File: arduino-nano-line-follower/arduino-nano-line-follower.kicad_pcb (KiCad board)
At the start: 2 copper layers, 0 parts

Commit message: project 9 / arduino nano line follower / added pcb
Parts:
- added 9V L298N: 9v_gnd_l293d, Connector_PinSocket_2.54mm:PinSocket_1x02_P2.54mm_Vertical, F.Cu at (112.8, 81.3)
- added A1: Arduino_Nano_Every, Module:Arduino_Nano, F.Cu at (93.5, 46.0)
- added ARD PWR: arduino_vcc_gnd, Connector_PinSocket_2.54mm:PinSocket_1x02_P2.54mm_Vertical, F.Cu at (112.8, 46.5)
- added BT1: Battery, Connector_PinSocket_2.54mm:PinSocket_1x02_P2.54mm_Vertical, F.Cu at (119.3, 81.2)
- added C1: 100n, Capacitor_THT:C_Disc_D3.0mm_W1.6mm_P2.50mm, F.Cu at (112.1, 60.2)
- added C2: 10u, Capacitor_THT:C_Radial_D4.0mm_H5.0mm_P1.50mm, F.Cu at (118.2, 75.9)
- added G***: LOGO, graphics:pcb_logo_3mmx3mm, F.Cu at (103.8, 38.8)
- added G***: LOGO, graphics:pcb_logo_45mmx45mm, B.Cu at (103.8, 64.4)
- added INP L298N: l298_input_pins, Connector_PinHeader_2.54mm:PinHeader_1x04_P2.54mm_Vertical, F.Cu at (89.6, 61.3)
- added IR PWR: 5v_ir_sensors_pins, Connector_PinHeader_2.54mm:PinHeader_1x02_P2.54mm_Vertical, F.Cu at (112.9, 56.6)
- added IR SIG: ir_signal, Connector_PinHeader_2.54mm:PinHeader_1x02_P2.54mm_Vertical, F.Cu at (112.8, 64.1)
- added PWR GND: gnd_ir_sensors_pins, Connector_PinHeader_2.54mm:PinHeader_1x02_P2.54mm_Vertical, F.Cu at (112.8, 51.6)
- added PWR SW: pwr_switch, Button_Switch_THT:SW_NKK_G1xJP, F.Cu at (115.0, 76.6)
- added REF**: MountingHole_3.2mm_M3, MountingHole:MountingHole_3.2mm_M3, F.Cu at (88.2, 91.4)
- added REF**: MountingHole_3.2mm_M3, MountingHole:MountingHole_3.2mm_M3, F.Cu at (120.4, 91.5)
- added REF**: MountingHole_3.2mm_M3, MountingHole:MountingHole_3.2mm_M3, F.Cu at (120.3, 38.4)
- added REF**: MountingHole_3.2mm_M3, MountingHole:MountingHole_3.2mm_M3, F.Cu at (88.3, 38.4)
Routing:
- net Net-(A1-+5V): track 0.00 -> 11.9 mm
- net Net-(A1-A0): track 0.00 -> 9.98 mm
- net +9V: track 0.00 -> 9.35 mm
- net Net-(A1-A1): track 0.00 -> 9.02 mm
- net Net-(J5-Pin_1): track 0.00 -> 4.80 mm
- net +5V: track 0.00 -> 4.34 mm
- net Net-(A1-D7): track 0.00 -> 3.88 mm
- net Net-(A1-D5): track 0.00 -> 3.88 mm
- net Net-(A1-D4): track 0.00 -> 3.88 mm
- net Net-(A1-D6): track 0.00 -> 3.88 mm
- added copper zone on B.Cu, net GND
- added copper zone on F.Cu, net GND
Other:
- board outline added: 39.5 x 60.2 mm
- board text added: "|ARDUINO NANO LINE FOLLOWER|"

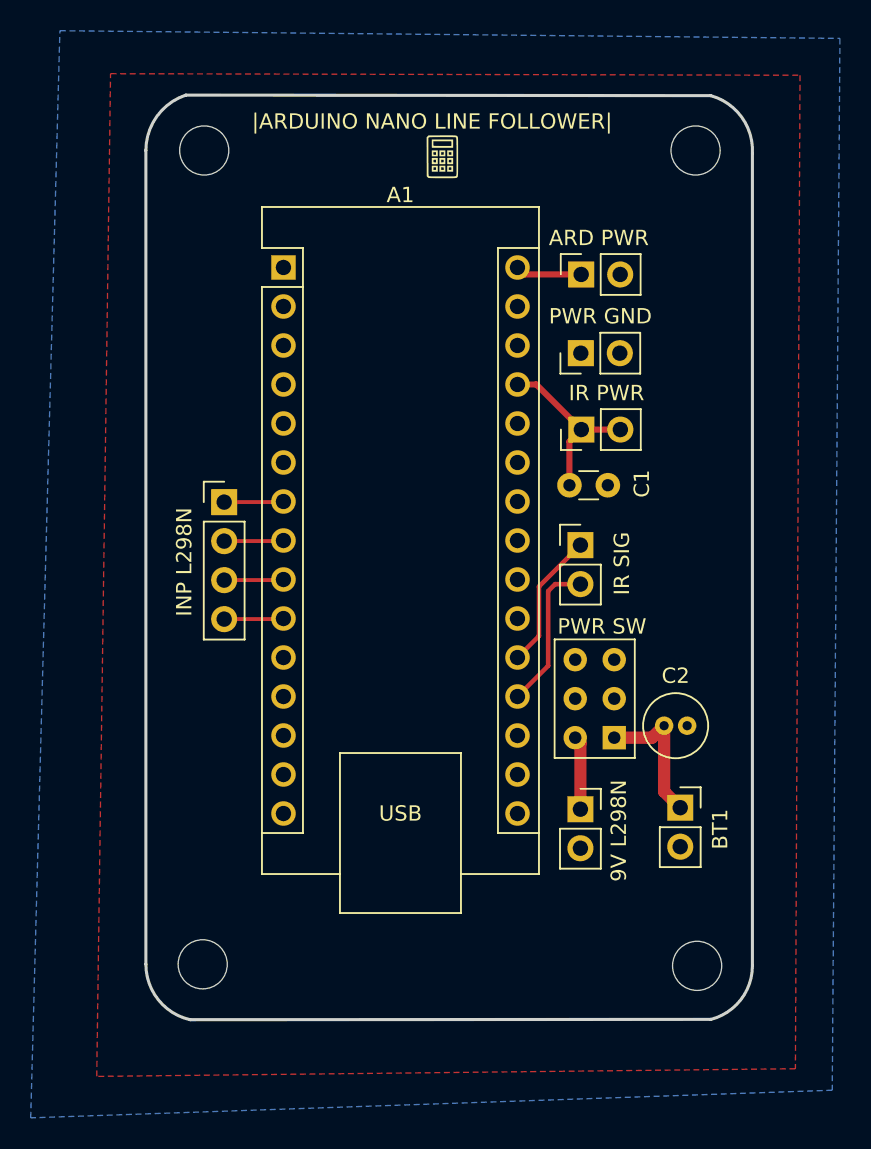
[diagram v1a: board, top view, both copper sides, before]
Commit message: project 9 / arduino nano line follower / improved connections
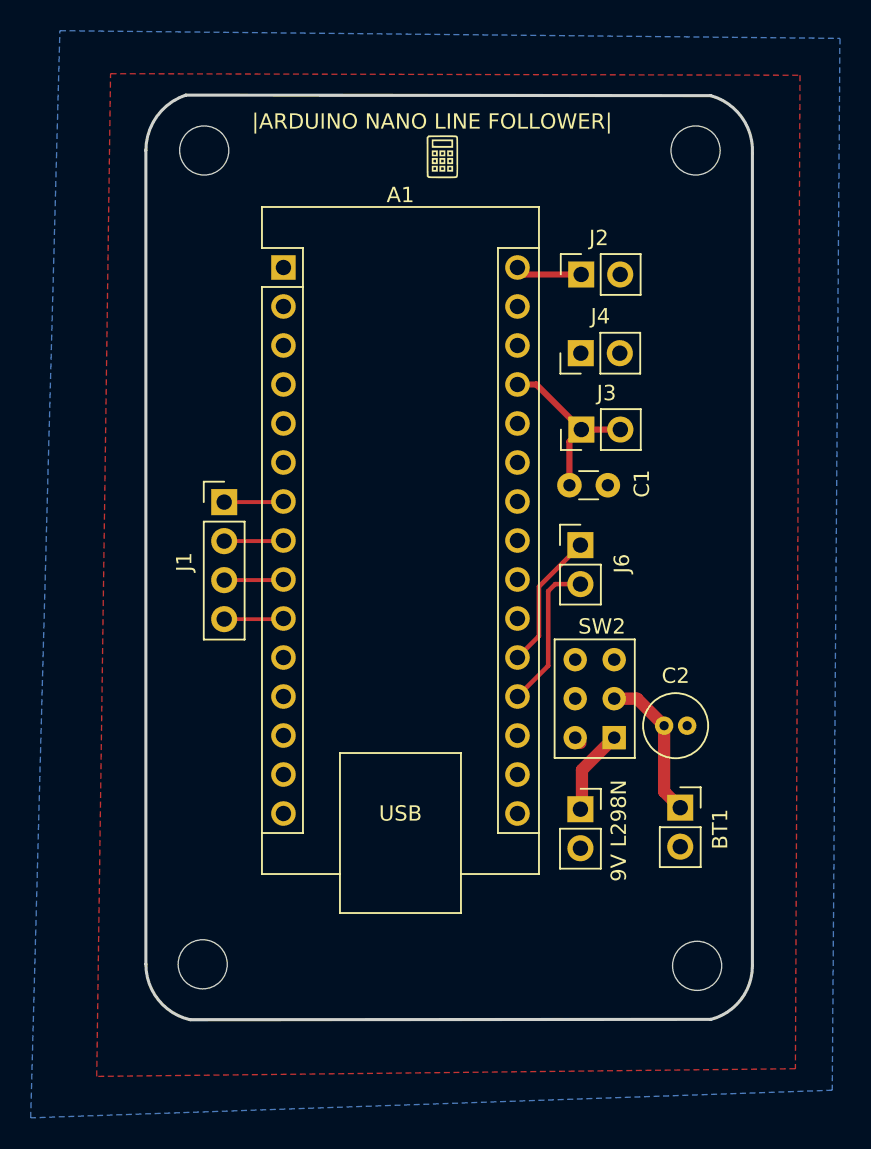
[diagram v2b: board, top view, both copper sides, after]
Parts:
- J1: renamed from INP L298N
- J2: renamed from ARD PWR
- J3: renamed from IR PWR
- J4: renamed from PWR GND
- J6: renamed from IR SIG
- SW2: renamed from PWR SW
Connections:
- SW2 pad 1: +9V -> Net-(J5-Pin_1)
- SW2 pad 2: unconnected-(SW2-Pad2) -> +9V
- SW2 pad 6: Net-(J5-Pin_1) -> unconnected-(SW2-Pad6)
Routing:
- net Net-(J5-Pin_1): track 4.80 -> 5.57 mm
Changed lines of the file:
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@@
   (net 30 "+9V")
   (net 31 "Net-(J5-Pin_1)")
-  (net 32 "unconnected-(SW2-Pad2)")
+  (net 32 "unconnected-(SW2-Pad6)")
   (net 33 "unconnected-(SW2-Pad3)")
   (net 34 "unconnected-(SW2-Pad4)")
@@
     (property "ki_keywords" "dip switch")
     (attr through_hole)
-    (fp_text reference "PWR SW" (at 0.8 7.24) (layer "F.SilkS")
+    (fp_text reference "SW2" (at 0.8 7.24) (layer "F.SilkS")
         (effects (font (size 1 1) (thickness 0.15)))
     )
@@
       (stroke (width 0.1) (type solid)) (layer "F.Fab"))
     (pad "1" thru_hole rect (at 0 0 180) (size 1.524 1.524) (drill 0.8128) (layers "*.Cu" "*.Mask")
+      (net 31 "Net-(J5-Pin_1)") (pintype "passive"))
+    (pad "2" thru_hole circle (at 0 2.54 180) (size 1.524 1.524) (drill 0.8128) (layers "*.Cu" "*.Mask")
       (net 30 "+9V") (pintype "passive"))
-    (pad "2" thru_hole circle (at 0 2.54 180) (size 1.524 1.524) (drill 0.8128) (layers "*.Cu" "*.Mask")
-      (net 32 "unconnected-(SW2-Pad2)") (pintype "passive+no_connect"))
     (pad "3" thru_hole circle (at 0 5.08 180) (size 1.524 1.524) (drill 0.8128) (layers "*.Cu" "*.Mask")
       (net 33 "unconnected-(SW2-Pad3)") (pintype "passive+no_connect"))
@@
       (net 35 "unconnected-(SW2-Pad5)") (pintype "passive+no_connect"))
     (pad "6" thru_hole circle (at 2.54 0 180) (size 1.524 1.524) (drill 0.8128) (layers "*.Cu" "*.Mask")
-      (net 31 "Net-(J5-Pin_1)") (pintype "passive"))
+      (net 32 "unconnected-(SW2-Pad6)") (pintype "passive+no_connect"))
     (model "${KICAD6_3DMODEL_DIR}/Button_Switch_THT.3dshapes/SW_NKK_G1xJP.wrl"
       (offset (xyz 0 0 0))
@@
     (property "ki_keywords" "connector")
     (attr through_hole)
-    (fp_text reference "IR SIG" (at 2.7 1.2 90) (layer "F.SilkS")
+    (fp_text reference "J6" (at 2.7 1.2 90) (layer "F.SilkS")
         (effects (font (size 1 1) (thickness 0.15)))
     )
@@
     (property "ki_keywords" "connector")
     (attr through_hole)
-    (fp_text reference "PWR GND" (at 2.4 1.275 180) (layer "F.SilkS")
+    (fp_text reference "J4" (at 2.4 1.275 180) (layer "F.SilkS")
         (effects (font (size 1 1) (thickness 0.15)))
     )
@@
     (property "ki_keywords" "connector")
     (attr through_hole)
-    (fp_text reference "INP L298N" (at -2.6 3.9 90) (layer "F.SilkS")
+    (fp_text reference "J1" (at -2.6 3.9 90) (layer "F.SilkS")
         (effects (font (size 1 1) (thickness 0.15)))
     )
@@
     (property "ki_keywords" "connector")
     (attr through_hole)
-    (fp_text reference "ARD PWR" (at 2.375 1.15 180) (layer "F.SilkS")
+    (fp_text reference "J2" (at 2.375 1.15 180) (layer "F.SilkS")
         (effects (font (size 1 1) (thickness 0.15)))
     )
@@
     (property "ki_keywords" "connector")
     (attr through_hole)
-    (fp_text reference "IR PWR" (at 2.375 1.64 180) (layer "F.SilkS")
+    (fp_text reference "J3" (at 2.375 1.64 180) (layer "F.SilkS")
         (effects (font (size 1 1) (thickness 0.15)))
     )
@@
   (segment (start 112.85 46.475) (end 109.155 46.475) (width 0.4) (layer "F.Cu") (net 29))
   (segment (start 109.155 46.475) (end 108.7 46.02) (width 0.4) (layer "F.Cu") (net 29))
-  (segment (start 117.47 76.64) (end 118.25 75.86) (width 0.8) (layer "F.Cu") (net 30))
   (segment (start 118.25 80.15) (end 118.25 75.86) (width 0.8) (layer "F.Cu") (net 30))
+  (segment (start 118.25 75.86) (end 116.49 74.1) (width 0.8) (layer "F.Cu") (net 30))
   (segment (start 119.3 81.2) (end 118.25 80.15) (width 0.8) (layer "F.Cu") (net 30))
-  (segment (start 115 76.64) (end 117.47 76.64) (width 0.8) (layer "F.Cu") (net 30))
-  (segment (start 112.8 76.98) (end 112.46 76.64) (width 0.8) (layer "F.Cu") (net 31))
-  (segment (start 112.8 81.3) (end 112.8 76.98) (width 0.8) (layer "F.Cu") (net 31))
+  (segment (start 116.49 74.1) (end 115 74.1) (width 0.8) (layer "F.Cu") (net 30))
+  (segment (start 112.9 81.2) (end 112.8 81.3) (width 0.8) (layer "F.Cu") (net 31))
+  (segment (start 112.9 78.74) (end 112.9 81.2) (width 0.8) (layer "F.Cu") (net 31))
+  (segment (start 115 76.64) (end 112.9 78.74) (width 0.8) (layer "F.Cu") (net 31))
+  (segment (start 112.8 76.98) (end 112.46 76.64) (width 0.8) (layer "F.Cu") (net 32))
   (zone (net 4) (net_name "GND") (layer "F.Cu") (hatch edge 0.5)
     (connect_pads (clearance 0.5))
